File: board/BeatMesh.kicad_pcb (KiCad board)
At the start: 2 copper layers, 100 x 100 mm, 75 parts, among them J1 AudioJack3_SwitchTR, J10 AudioJack3_SwitchTR, J12 MIDI IN, J13 USB POWER, J14 Conn_01x04_Pin, J15 MIDI GND, J16 Conn_01x02, J17 CV CLOCK OUT, J18 CV PLAY-STOP OUT, J19 3.3V,21,22,27,35,GND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

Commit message: errata V1 + updated to kicad 10
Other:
- board text added: "GND,VCC"
- board text removed: "VCC,GND"

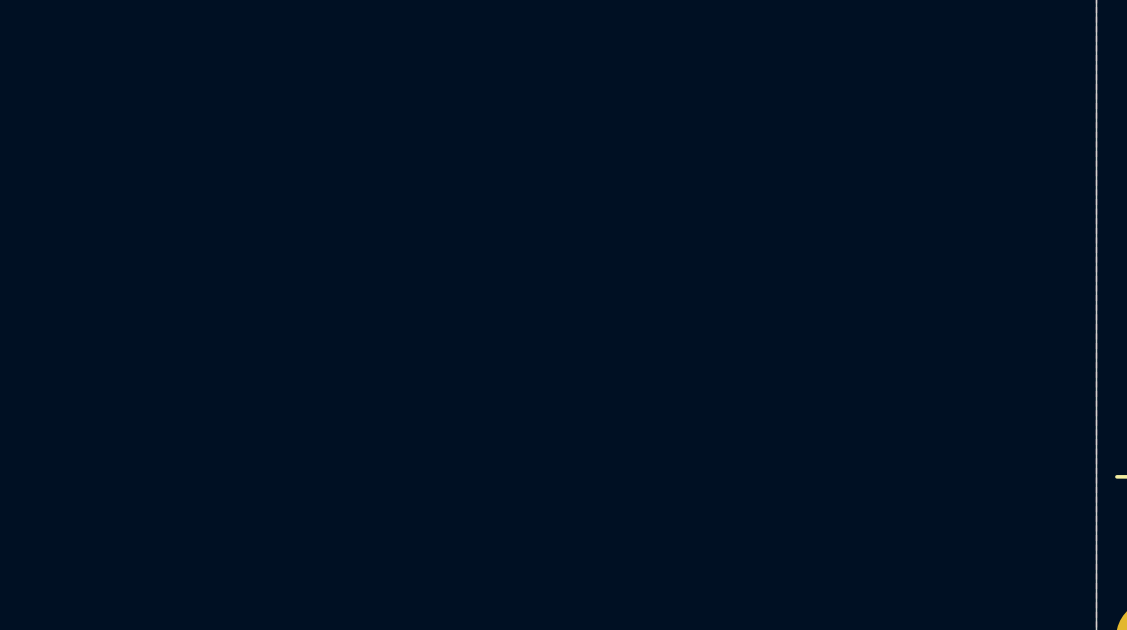
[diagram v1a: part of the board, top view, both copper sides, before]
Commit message: modulo for ppqn, added TODO in pcb
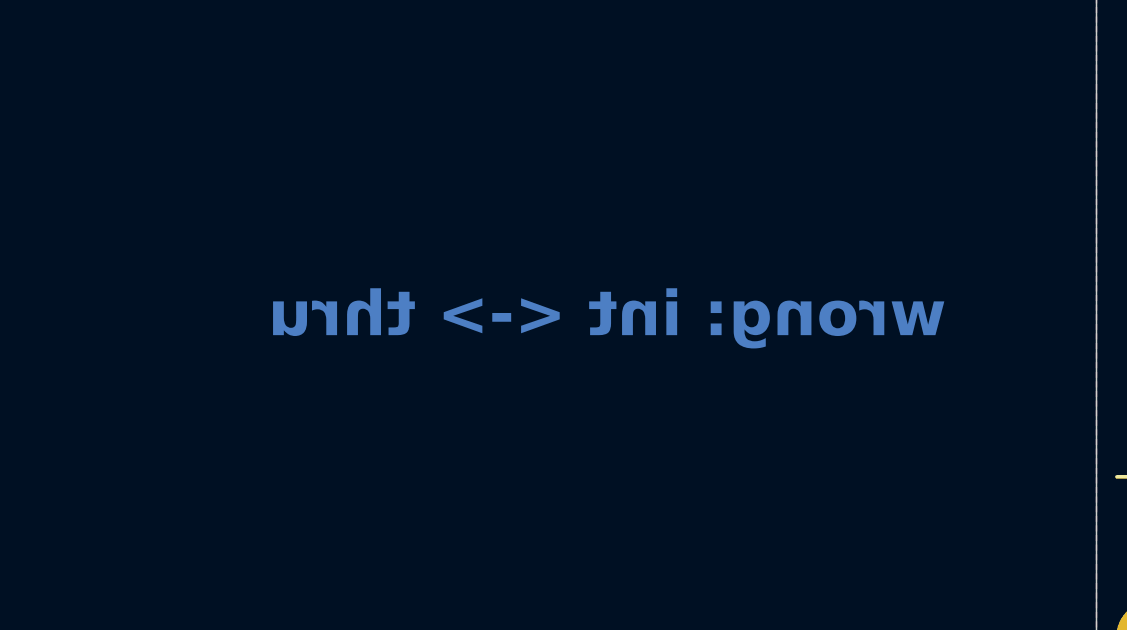
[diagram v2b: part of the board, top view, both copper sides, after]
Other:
- board text added: "wrong: int <-> thru"
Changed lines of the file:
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@@
 		(43 "User.3" user)
 		(45 "User.4" user)
+		(49 "User.6" user)
 	)
 	(setup
@@
 		(layer "Edge.Cuts")
 	)
+	(gr_line
+		(start 95.55065 48.8498)
+		(end 95.55065 148.8498)
+		(stroke
+			(width 0.1)
+			(type default)
+		)
+		(layer "User.6")
+	)
+	(gr_line
+		(start 95.55065 48.8498)
+		(end 195.55065 48.8498)
+		(stroke
+			(width 0.1)
+			(type default)
+		)
+		(layer "User.6")
+	)
+	(gr_line
+		(start 195.55065 48.8498)
+		(end 195.55065 148.8498)
+		(stroke
+			(width 0.1)
+			(type default)
+		)
+		(layer "User.6")
+	)
+	(gr_line
+		(start 195.55065 148.8498)
+		(end 95.55065 148.8498)
+		(stroke
+			(width 0.1)
+			(type default)
+		)
+		(layer "User.6")
+	)
+	(gr_text "wrong: int <-> thru"
+		(at 90.55065 63.4498 0)
+		(layer "B.Cu")
+		(effects
+			(font
+				(size 1.5 1.5)
+				(thickness 0.3)
+				(bold yes)
+			)
+			(justify left bottom mirror)
+		)
+	)
 	(gr_text "v1 - 02/2026"

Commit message: board v2
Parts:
- removed ?: , clipboard:595ac4dd-d3f5-405d-b7c1-3865580d633b
- removed DH1, DH2, DH3, DH4: MountingHole_3.2mm_M3_Pad_Via, MountingHole:MountingHole_3.2mm_M3_Pad_Via
- removed J18: CV PLAY-STOP OUT, AudioConnectorFixed:BeatMeshJack_3.5mm_CUI_SJ1-3515N_Horizontal
- removed J19: 3.3V,21,22,27,35,GND, Connector_PinHeader_2.54mm:PinHeader_1x06_P2.54mm_Vertical
- removed R27: 1K, Resistor_THT:R_Axial_DIN0204_L3.6mm_D1.6mm_P5.08mm_Horizontal
- added G***: LOGO, BaldApproved:baldapproved, B.Cu at (143.5, 111.7)
- added J11: Conn_01x05_Pin, Connector_PinHeader_2.54mm:PinHeader_1x05_P2.54mm_Vertical, F.Cu at (159.8, 136.1)
- added REF1: MountingHole_3.2mm_M3_Pad_Via, MountingHole:MountingHole_3.2mm_M3_Pad_Via, F.Cu at (190.6, 53.8)
- added REF2: MountingHole_3.2mm_M3_Pad_Via, MountingHole:MountingHole_3.2mm_M3_Pad_Via, F.Cu at (100.6, 53.8)
- added REF3: MountingHole_3.2mm_M3_Pad_Via, MountingHole:MountingHole_3.2mm_M3_Pad_Via, F.Cu at (190.6, 143.8)
- added REF4: MountingHole_3.2mm_M3_Pad_Via, MountingHole:MountingHole_3.2mm_M3_Pad_Via, F.Cu at (100.6, 143.8)
- J12: value MIDI IN -> DIN-5_180degree
- J13: value USB POWER -> USB_C_Receptacle_USB2.0_16P; footprint Connector_USB:USB_C_Receptacle_GCT_USB4085 -> Connector_USB:USB_C_Receptacle_HRO_TYPE-C-31-M-12
- J15: value MIDI GND -> Conn_01x02
- J17: value CV CLOCK OUT -> AudioJack3_SwitchTR
- J2: value CV RESET OUT -> AudioJack3_SwitchTR
- J20: value MIDI IN -> AudioJack3_SwitchTR
- J23: value CV CLOCK IN -> AudioJack3_SwitchTR
- J24, J5: value MIDI OUT -> AudioJack3_SwitchTR
- J9: footprint Connector_Audio:Jack_3.5mm_CUI_SJ1-3515N_Horizontal -> AudioConnectorFixed:BeatMeshJack_3.5mm_CUI_SJ1-3515N_Horizontal
- Q1: footprint Package_TO_SOT_THT:TO-92_Inline -> Package_TO_SOT_THT:TO-92_Inline_Wide
- moved J17 5.50 mm to (129.6, 147.0)
- moved J2 5.50 mm to (143.6, 147.0)
- moved J13 5.46 mm to (180.2, 51.1)
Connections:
- SW1 pad 1: /ESP32_TX -> /MIDI_IN
- SW1 pad 3: /MIDI_IN -> /ESP32_TX
- U4 pad 5: /IO27_CV_PLAYSTOP -> (no net)
- U4 pad 6: Net-(R27-Pad1) -> (no net)
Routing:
- net GND: track 370.5 -> 0.00 mm, vias 1 -> 0
- net /IO27_CV_PLAYSTOP: track 41.8 -> 0.00 mm
- net Net-(J18-PadT): track 35.9 -> 0.00 mm, vias 1 -> 0
- net /IO21_CV_RESET: track 29.5 -> 0.00 mm
- net Net-(R27-Pad1): track 21.3 -> 0.00 mm
- net /ESP32_RX: track 136.6 -> 115.4 mm, vias 1 -> 0
- net /IO35: track 103.6 -> 84.7 mm, vias 1 -> 0
- net Net-(D1-K): track 69.2 -> 55.2 mm
- net Net-(R6-Pad1): track 21.7 -> 35.6 mm
- net /ESP32_TX: track 128.6 -> 139.9 mm
- net /MIDI_IN: track 105.1 -> 96.0 mm
- net Net-(J13-CC2): track 12.0 -> 4.24 mm
- net /SLEEVE: track 256.5 -> 249.1 mm, vias 1 -> 0
- net Net-(J24-PadT): track 75.8 -> 82.9 mm
- net Net-(J5-PadT): track 74.4 -> 80.8 mm
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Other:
- board text added: "3.3v, io22, io27, io35, gnd"
- board text added: "CV CLOCK"
- board text added: "CV CLOCK IN"
- board text added: "CV CLOCK, RESET, CV IN"
- board text added: "CV RESET"
- board text added: "INT <-> THRU"
- board text added: "MIDI IN"
- board text added: "v2 - 02/2026"
- board text removed: "THRU <-> INT"
- board text removed: "v1 - 02/2026"
- board text removed: "wrong: int <-> thru"
